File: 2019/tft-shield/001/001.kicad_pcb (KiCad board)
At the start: 2 copper layers, 6 parts, among them J1 CONN_01X08, Q1 S8050

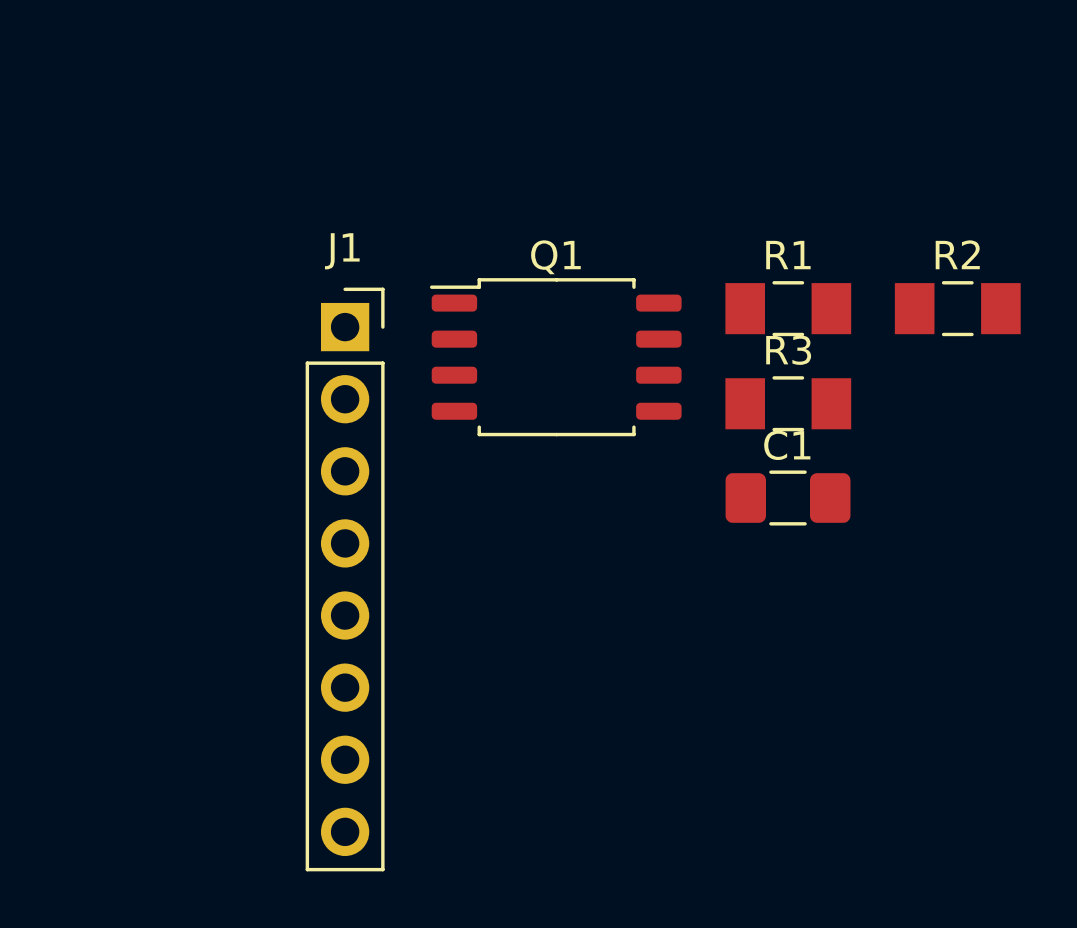
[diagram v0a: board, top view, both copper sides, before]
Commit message: Add Draw settings in Docs TFT
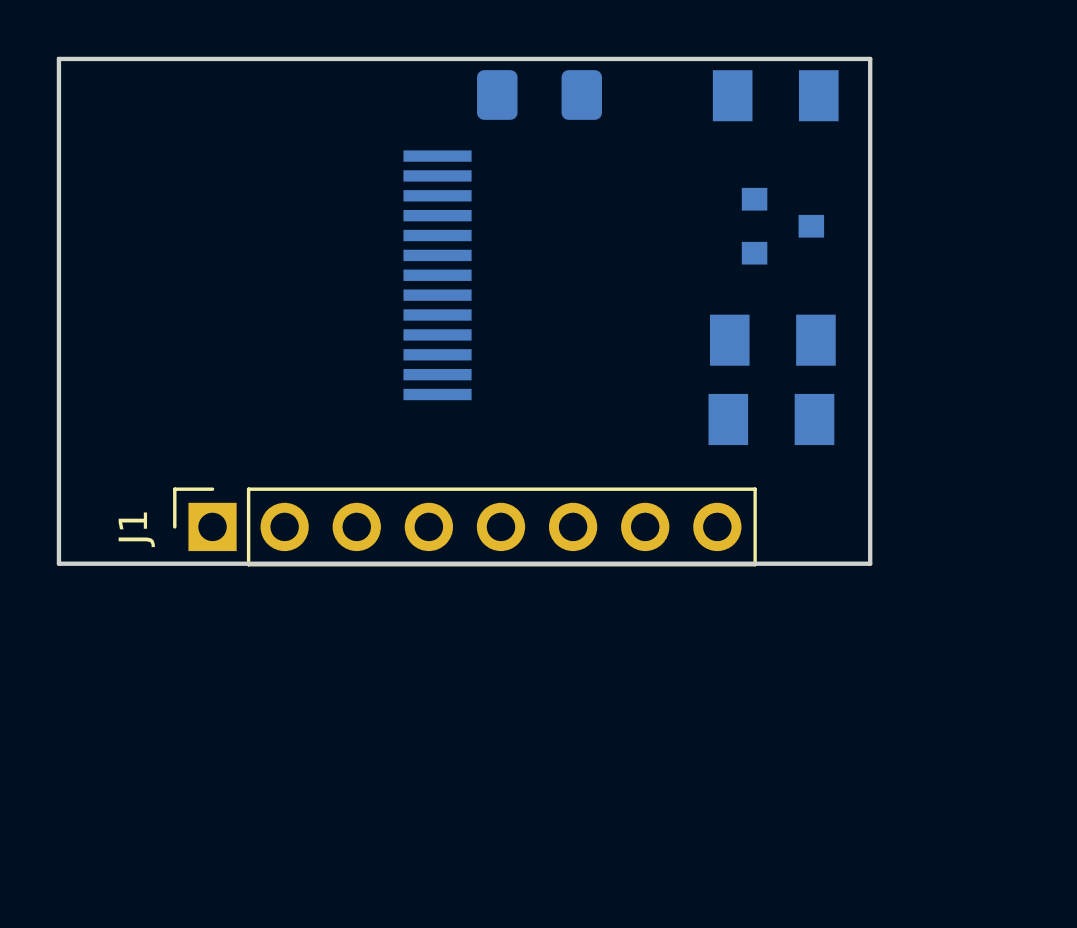
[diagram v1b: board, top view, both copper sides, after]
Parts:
- added U1: TFT_0.9680*160, tft-shield:TFT_0.96_SPI, B.Cu at (137.8, 89.5)
- C1, R1, R2, R3: moved to B.Cu
- Q1: footprint Package_SO:SOIC-8_5.23x5.23mm_P1.27mm -> Package_TO_SOT_SMD:SOT-23; moved to B.Cu
- moved C1 16.7 mm to (141.4, 83.2), turned to 180 degrees
- moved R3 10.9 mm to (149.7, 83.2)
- moved Q1 9.21 mm to (150.0, 87.8)
- moved J1 8.45 mm to (129.9, 98.4), turned to 90 degrees
- moved R2 7.64 mm to (149.6, 94.6)
- moved R1 1.24 mm to (149.6, 91.8)
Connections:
- J1 pad 3: /SCL -> /BLK
- J1 pad 4: /SDA -> /CS
- J1 pad 7: /CS -> /SCL
- J1 pad 8: /BLK -> /SDA
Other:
- board outline added: 28.6 x 17.8 mm
